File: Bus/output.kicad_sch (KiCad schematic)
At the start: 3 parts, among them J12 Conn_01x07_Pin, J13 Conn_01x08_Pin, J14 Conn_01x08_Pin

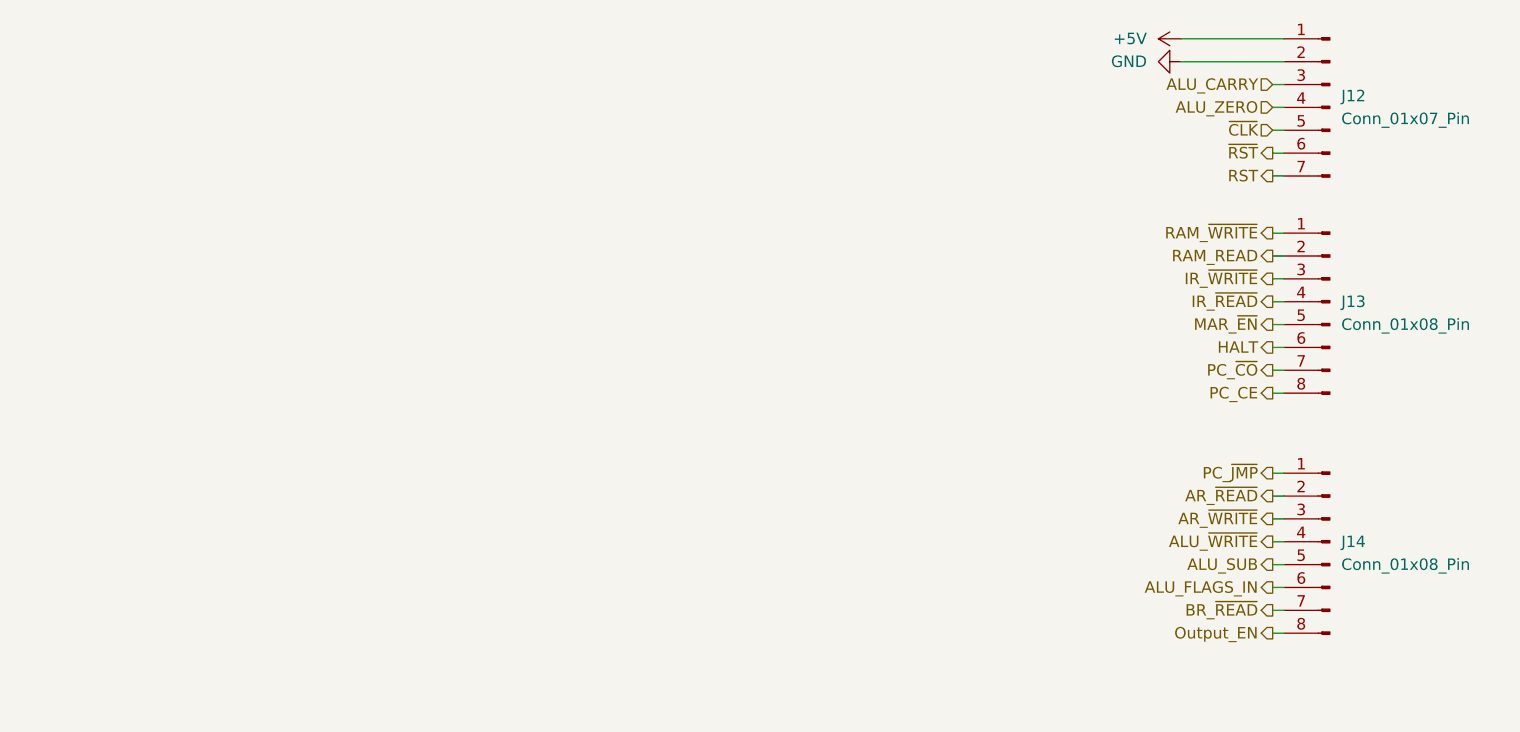
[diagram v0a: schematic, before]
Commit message: Updated bus schmatic pins to match final layouts
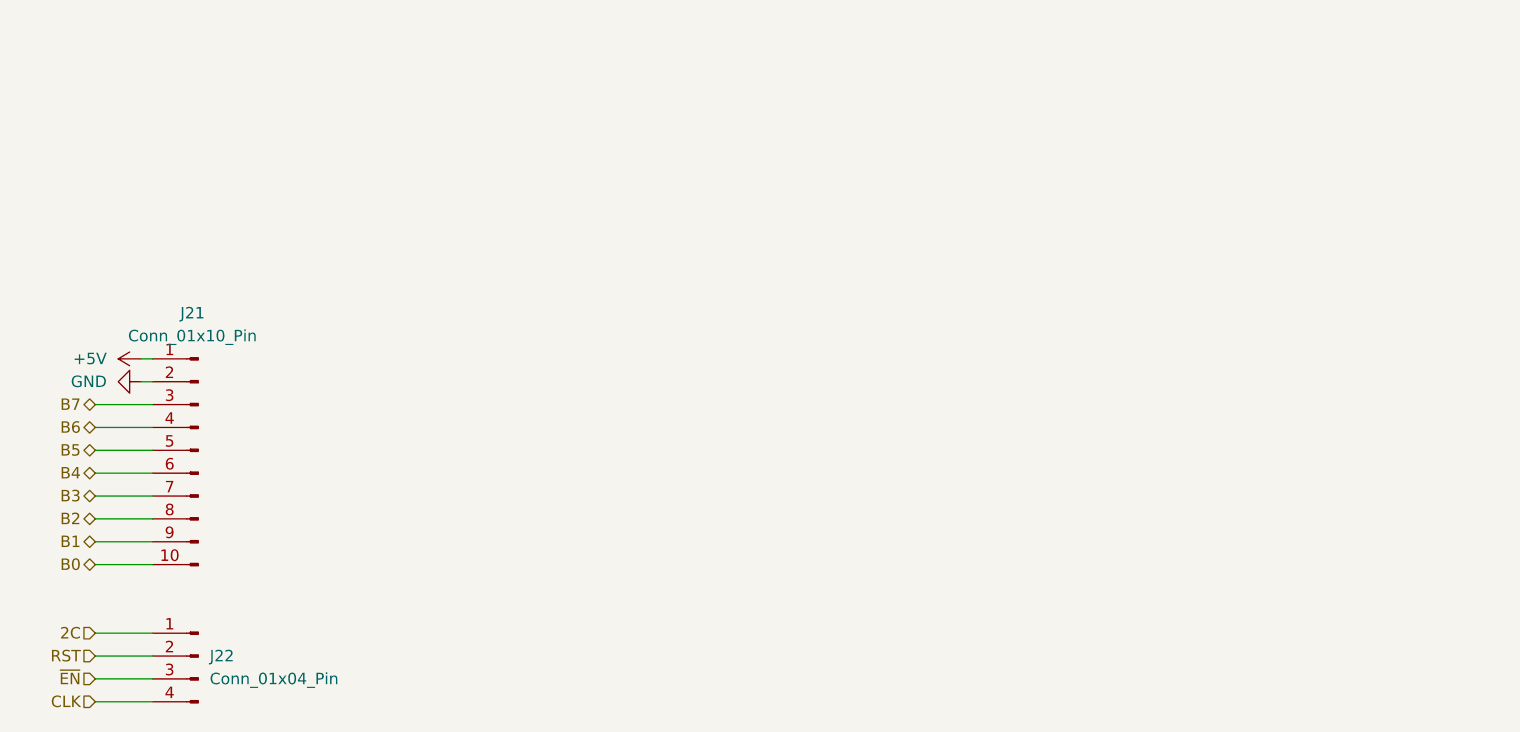
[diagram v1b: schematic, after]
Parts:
- removed J12: Conn_01x07_Pin, Connector_PinHeader_2.54mm:PinHeader_1x07_P2.54mm_Vertical, symbol Connector:Conn_01x07_Pin
- removed J13, J14: Conn_01x08_Pin, Connector_PinHeader_2.54mm:PinHeader_1x08_P2.54mm_Vertical, symbol Connector:Conn_01x08_Pin
- added J21: Conn_01x10_Pin, Connector_PinHeader_2.54mm:PinHeader_1x10_P2.54mm_Vertical, symbol Connector:Conn_01x10_Pin
- added J22: Conn_01x04_Pin, Connector_PinHeader_2.54mm:PinHeader_1x04_P2.54mm_Vertical, symbol Connector:Conn_01x04_Pin
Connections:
- net +5V: now also J21.1 (Pin_1)
- net GND: now also J21.2 (Pin_2)
- net RST: now also J22.2 (Pin_2)
- new net 2C: J22.1 (Pin_1)
- new net B0: J21.10 (Pin_10)
- new net B1: J21.9 (Pin_9)
- new net B2: J21.8 (Pin_8)
- new net B3: J21.7 (Pin_7)
- new net B4: J21.6 (Pin_6)
- new net B5: J21.5 (Pin_5)
- new net B6: J21.4 (Pin_4)
- new net B7: J21.3 (Pin_3)
- new net CLK: J22.4 (Pin_4)
- new net ~{EN}: J22.3 (Pin_3)

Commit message: Ouput bus was labeled incorectly. Labels fixed on output. Labels and connections fixed on bus
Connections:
- net B0: now also J21.3 (Pin_3); no longer J21.10 (Pin_10)
- net B1: now also J21.4 (Pin_4); no longer J21.9 (Pin_9)
- net B2: now also J21.5 (Pin_5); no longer J21.8 (Pin_8)
- net B3: now also J21.6 (Pin_6); no longer J21.7 (Pin_7)
- net B4: now also J21.7 (Pin_7); no longer J21.6 (Pin_6)
- net B5: now also J21.8 (Pin_8); no longer J21.5 (Pin_5)
- net B6: now also J21.9 (Pin_9); no longer J21.4 (Pin_4)
- net B7: now also J21.10 (Pin_10); no longer J21.3 (Pin_3)
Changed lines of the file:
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@@
 	(hierarchical_label "B1"
 		(shape bidirectional)
-		(at 68.58 105.41 180)
+		(at 68.58 92.71 180)
 		(fields_autoplaced yes)
 		(effects
@@
 	(hierarchical_label "B5"
 		(shape bidirectional)
-		(at 68.58 95.25 180)
+		(at 68.58 102.87 180)
 		(fields_autoplaced yes)
 		(effects
@@
 	(hierarchical_label "B2"
 		(shape bidirectional)
-		(at 68.58 102.87 180)
+		(at 68.58 95.25 180)
 		(fields_autoplaced yes)
 		(effects
@@
 	(hierarchical_label "B4"
 		(shape bidirectional)
-		(at 68.58 97.79 180)
+		(at 68.58 100.33 180)
 		(fields_autoplaced yes)
 		(effects
@@
 	(hierarchical_label "B0"
 		(shape bidirectional)
-		(at 68.58 107.95 180)
+		(at 68.58 90.17 180)
 		(fields_autoplaced yes)
 		(effects
@@
 	(hierarchical_label "B3"
 		(shape bidirectional)
-		(at 68.58 100.33 180)
+		(at 68.58 97.79 180)
 		(fields_autoplaced yes)
 		(effects
@@
 	(hierarchical_label "B6"
 		(shape bidirectional)
-		(at 68.58 92.71 180)
+		(at 68.58 105.41 180)
 		(fields_autoplaced yes)
 		(effects
@@
 	(hierarchical_label "B7"
 		(shape bidirectional)
-		(at 68.58 90.17 180)
+		(at 68.58 107.95 180)
 		(fields_autoplaced yes)
 		(effects
